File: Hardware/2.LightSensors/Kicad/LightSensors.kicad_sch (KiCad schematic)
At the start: 20 parts, among them J1 Conn_01x10_Pin, U1 AS7331, U2 OPT3004

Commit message: update footprints
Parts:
- H1, H2, H3, H4: footprint MountingHole:MountingHole_3.2mm_M3_ISO7380 -> MountingHole:MountingHole_3.2mm_M3
- J1: footprint Connector_JST:JST_PH_S10B-PH-K_1x10_P2.00mm_Horizontal -> Connector_JST:JST_PH_B10B-PH-SM4-TB_1x10-1MP_P2.00mm_Vertical
- R3, R6: footprint Capacitor_SMD:C_0402_1005Metric -> Resistor_SMD:R_0402_1005Metric
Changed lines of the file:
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@@
-    )
-  )
-  (symbol (lib_id "Mechanical:MountingHole") (at 64.77 193.04 0) (unit 1)
-    (in_bom yes) (on_board yes) (dnp no) (fields_autoplaced)
-    (property "Reference" "H2" (at 67.31 191.77 0)
-      (effects (font (size 1.27 1.27)) (justify left))
-    )
-    (property "Value" "MountingHole" (at 67.31 194.31 0)
-      (effects (font (size 1.27 1.27)) (justify left) hide)
-    )
-    (property "Footprint" "MountingHole:MountingHole_3.2mm_M3_ISO7380" (at 64.77 193.04 0)
-      (effects (font (size 1.27 1.27)) hide)
-    )
-    (property "Datasheet" "~" (at 64.77 193.04 0)
-      (effects (font (size 1.27 1.27)) hide)
-    )
-    (instances
-      (project "LightSensors"
-        (path "/23129930-610b-43a1-9ece-3793e6901ef4"
-          (reference "H2") (unit 1)
-        )
-      )
     )
   )
@@
     )
   )
-  (symbol (lib_id "Mechanical:MountingHole") (at 73.66 193.04 0) (unit 1)
-    (in_bom yes) (on_board yes) (dnp no) (fields_autoplaced)
-    (property "Reference" "H4" (at 76.2 191.77 0)
-      (effects (font (size 1.27 1.27)) (justify left))
-    )
-    (property "Value" "MountingHole" (at 76.2 194.31 0)
-      (effects (font (size 1.27 1.27)) (justify left) hide)
-    )
-    (property "Footprint" "MountingHole:MountingHole_3.2mm_M3_ISO7380" (at 73.66 193.04 0)
-      (effects (font (size 1.27 1.27)) hide)
-    )
-    (property "Datasheet" "~" (at 73.66 193.04 0)
-      (effects (font (size 1.27 1.27)) hide)
-    )
-    (instances
-      (project "LightSensors"
-        (path "/23129930-610b-43a1-9ece-3793e6901ef4"
-          (reference "H4") (unit 1)
-        )
-      )
-    )
-  )
   (symbol (lib_id "Device:C") (at 213.36 55.88 0) (unit 1)
     (in_bom yes) (on_board yes) (dnp no) (fields_autoplaced)
@@
         (path "/e35789fa-b5f2-47cd-8637-9150d2b422dd"
           (reference "C1") (unit 1)
+        )
+      )
+    )
+  )
+  (symbol (lib_id "Mechanical:MountingHole") (at 83.82 184.15 0) (unit 1)
+    (in_bom yes) (on_board yes) (dnp no) (fields_autoplaced)
+    (property "Reference" "H3" (at 86.36 182.88 0)
+      (effects (font (size 1.27 1.27)) (justify left))
+    )
+    (property "Value" "MountingHole" (at 86.36 185.42 0)
+      (effects (font (size 1.27 1.27)) (justify left))
+    )
+    (property "Footprint" "MountingHole:MountingHole_3.2mm_M3" (at 83.82 184.15 0)
+      (effects (font (size 1.27 1.27)) hide)
+    )
+    (property "Datasheet" "~" (at 83.82 184.15 0)
+      (effects (font (size 1.27 1.27)) hide)
+    )
+    (instances
+      (project "LightSensors"
+        (path "/23129930-610b-43a1-9ece-3793e6901ef4"
+          (reference "H3") (unit 1)
         )
       )
@@
     )
   )
+  (symbol (lib_id "Mechanical:MountingHole") (at 83.82 190.5 0) (unit 1)
+    (in_bom yes) (on_board yes) (dnp no) (fields_autoplaced)
+    (property "Reference" "H4" (at 86.36 189.23 0)
+      (effects (font (size 1.27 1.27)) (justify left))
+    )
+    (property "Value" "MountingHole" (at 86.36 191.77 0)
+      (effects (font (size 1.27 1.27)) (justify left))
+    )
+    (property "Footprint" "MountingHole:MountingHole_3.2mm_M3" (at 83.82 190.5 0)
+      (effects (font (size 1.27 1.27)) hide)
+    )
+    (property "Datasheet" "~" (at 83.82 190.5 0)
+      (effects (font (size 1.27 1.27)) hide)
+    )
+    (instances
+      (project "LightSensors"
+        (path "/23129930-610b-43a1-9ece-3793e6901ef4"
+          (reference "H4") (unit 1)
+        )
+      )
+    )
+  )
   (symbol (lib_id "power:+3.3V") (at 220.98 48.26 0) (unit 1)
     (in_bom yes) (on_board yes) (dnp no) (fields_autoplaced)
@@
     )
   )
-  (symbol (lib_id "Mechanical:MountingHole") (at 73.66 185.42 0) (unit 1)
-    (in_bom yes) (on_board yes) (dnp no) (fields_autoplaced)
-    (property "Reference" "H3" (at 76.2 184.15 0)
-      (effects (font (size 1.27 1.27)) (justify left))
-    )
-    (property "Value" "MountingHole" (at 76.2 186.69 0)
-      (effects (font (size 1.27 1.27)) (justify left) hide)
-    )
-    (property "Footprint" "MountingHole:MountingHole_3.2mm_M3_ISO7380" (at 73.66 185.42 0)
-      (effects (font (size 1.27 1.27)) hide)
-    )
-    (property "Datasheet" "~" (at 73.66 185.42 0)
-      (effects (font (size 1.27 1.27)) hide)
-    )
-    (instances
-      (project "LightSensors"
-        (path "/23129930-610b-43a1-9ece-3793e6901ef4"
-          (reference "H3") (unit 1)
-        )
-      )
-    )
-  )
   (symbol (lib_id "power:+3.3VA") (at 83.82 31.75 0) (unit 1)
     (in_bom yes) (on_board yes) (dnp no) (fields_autoplaced)
@@
       (effects (font (size 1.27 1.27)) (justify left))
     )
-    (property "Footprint" "Capacitor_SMD:C_0402_1005Metric" (at 254.762 44.45 90)
+    (property "Footprint" "Resistor_SMD:R_0402_1005Metric" (at 254.762 44.45 90)
       (effects (font (size 1.27 1.27)) hide)
     )
@@
     )
   )
+  (symbol (lib_id "Mechanical:MountingHole") (at 64.77 184.15 0) (unit 1)
+    (in_bom yes) (on_board yes) (dnp no) (fields_autoplaced)
+    (property "Reference" "H1" (at 67.31 182.88 0)
+      (effects (font (size 1.27 1.27)) (justify left))
+    )
+    (property "Value" "MountingHole" (at 67.31 185.42 0)
+      (effects (font (size 1.27 1.27)) (justify left))
+    )
+    (property "Footprint" "MountingHole:MountingHole_3.2mm_M3" (at 64.77 184.15 0)
+      (effects (font (size 1.27 1.27)) hide)
+    )
+    (property "Datasheet" "~" (at 64.77 184.15 0)
+      (effects (font (size 1.27 1.27)) hide)
+    )
+    (instances
+      (project "LightSensors"
+        (path "/23129930-610b-43a1-9ece-3793e6901ef4"
+          (reference "H1") (unit 1)
+        )
+      )
+    )
+  )
   (symbol (lib_id "power:+3.3VA") (at 95.25 31.75 0) (unit 1)
     (in_bom yes) (on_board yes) (dnp no) (fields_autoplaced)
@@
       (effects (font (size 1.27 1.27)) (justify left))
     )
-    (property "Footprint" "Capacitor_SMD:C_0402_1005Metric" (at 123.952 54.61 90)
+    (property "Footprint" "Resistor_SMD:R_0402_1005Metric" (at 123.952 54.61 90)
       (effects (font (size 1.27 1.27)) hide)
     )
@@
     )
   )
-  (symbol (lib_id "Mechanical:MountingHole") (at 64.77 185.42 0) (unit 1)
-    (in_bom yes) (on_board yes) (dnp no) (fields_autoplaced)
-    (property "Reference" "H1" (at 67.31 184.15 0)
-      (effects (font (size 1.27 1.27)) (justify left))
-    )
-    (property "Value" "MountingHole" (at 67.31 186.69 0)
-      (effects (font (size 1.27 1.27)) (justify left) hide)
-    )
-    (property "Footprint" "MountingHole:MountingHole_3.2mm_M3_ISO7380" (at 64.77 185.42 0)
-      (effects (font (size 1.27 1.27)) hide)
-    )
-    (property "Datasheet" "~" (at 64.77 185.42 0)
-      (effects (font (size 1.27 1.27)) hide)
-    )
-    (instances
-      (project "LightSensors"
-        (path "/23129930-610b-43a1-9ece-3793e6901ef4"
-          (reference "H1") (unit 1)
-        )
-      )
-    )
-  )
   (symbol (lib_id "Device:R") (at 170.18 71.12 270) (unit 1)
     (in_bom yes) (on_board yes) (dnp no)
@@
       (effects (font (size 1.27 1.27)) hide)
     )
-    (property "Footprint" "Connector_JST:JST_PH_S10B-PH-K_1x10_P2.00mm_Horizontal" (at 25.4 52.07 0)
+    (property "Footprint" "Connector_JST:JST_PH_B10B-PH-SM4-TB_1x10-1MP_P2.00mm_Vertical" (at 25.4 52.07 0)
       (effects (font (size 1.27 1.27)) hide)
     )
@@
         )
       )
+    )
+  )
+  (symbol (lib_id "Mechanical:MountingHole") (at 64.77 190.5 0) (unit 1)
+    (in_bom yes) (on_board yes) (dnp no) (fields_autoplaced)
+    (property "Reference" "H2" (at 67.31 189.23 0)
+      (effects (font (size 1.27 1.27)) (justify left))
+    )
+    (property "Value" "MountingHole" (at 67.31 191.77 0)
+      (effects (font (size 1.27 1.27)) (justify left))
+    )
+    (property "Footprint" "MountingHole:MountingHole_3.2mm_M3" (at 64.77 190.5 0)
+      (effects (font (size 1.27 1.27)) hide)
+    )
+    (property "Datasheet" "~" (at 64.77 190.5 0)
+      (effects (font (size 1.27 1.27)) hide)
+    )
+    (instances
+      (project "LightSensors"
+        (path "/23129930-610b-43a1-9ece-3793e6901ef4"
+          (reference "H2") (unit 1)
+        )
+      )

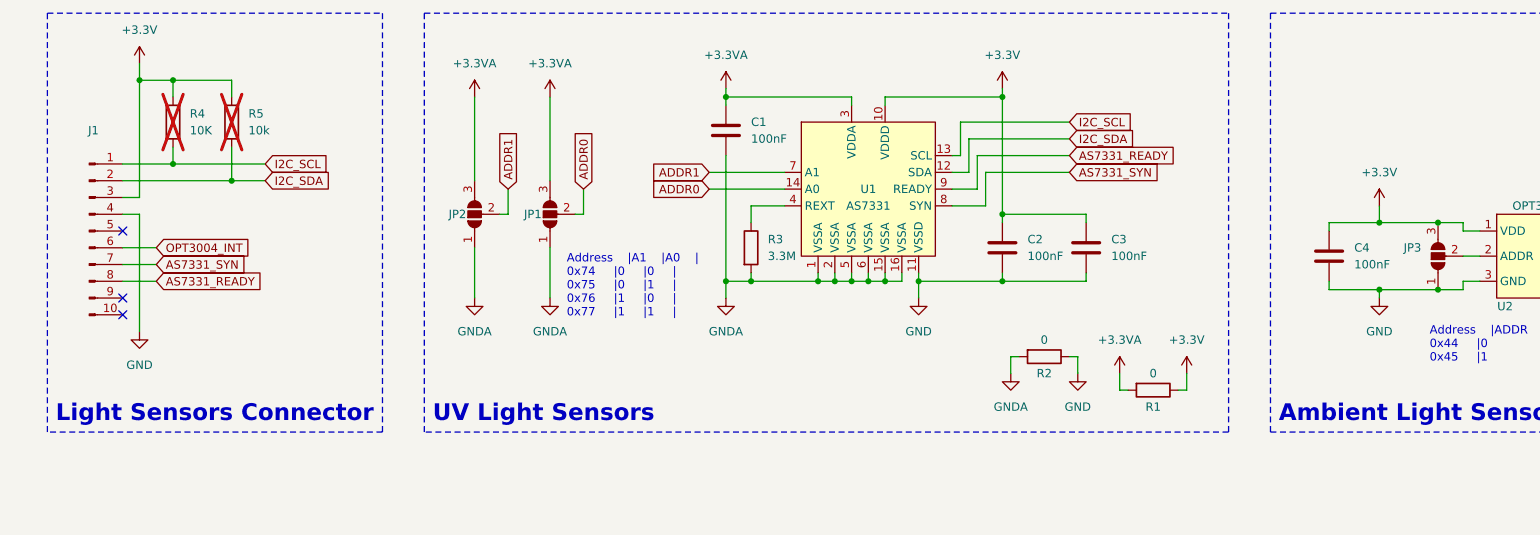
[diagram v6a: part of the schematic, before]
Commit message: Update pcb due to connector pinout fix
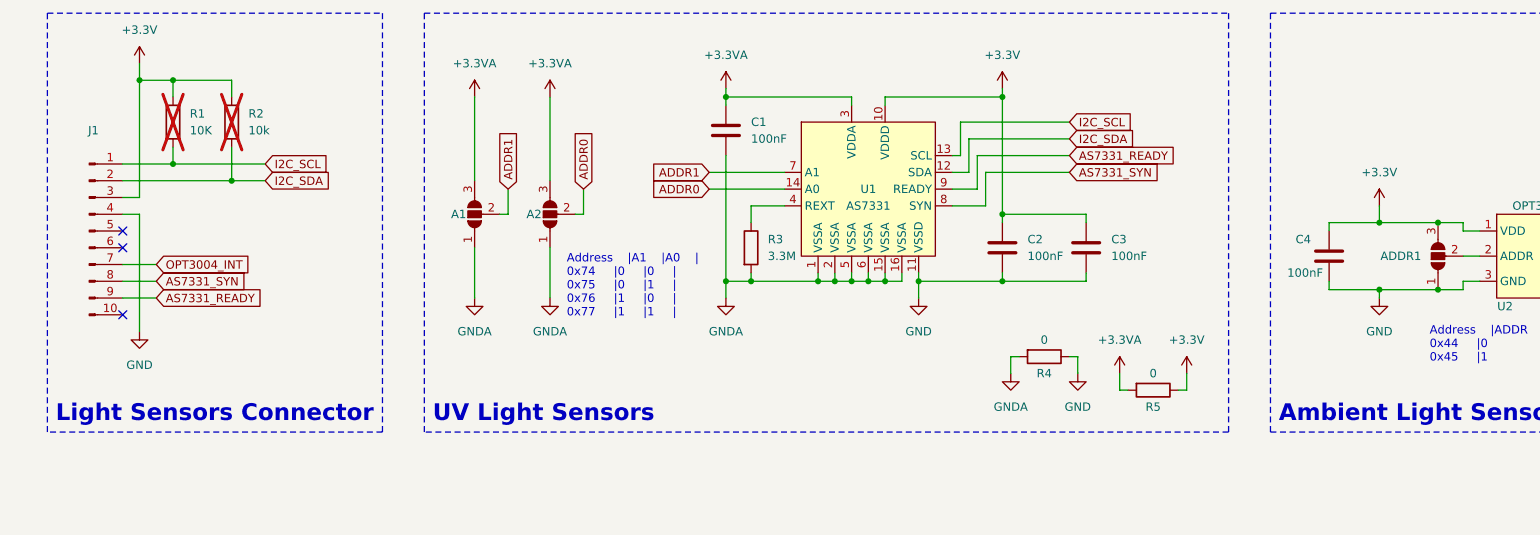
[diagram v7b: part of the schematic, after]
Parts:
- renumbered JP2 to A1, JP1 to A2, JP3 to ADDR1, R4 to R1, R5 to R2, R2 to R4, R1 to R5
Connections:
- net AS7331_READY: now also J1.9 (Pin_9); no longer J1.8 (Pin_8)
- net AS7331_SYN: now also J1.8 (Pin_8); no longer J1.7 (Pin_7)
- net OPT3004_INT: now also J1.7 (Pin_7); no longer J1.6 (Pin_6)

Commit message: Change footprints for resistors, capasitors and change mounting holes to M2
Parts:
- C1, C2, C3, C4: footprint Capacitor_SMD:C_0402_1005Metric -> Capacitor_SMD:C_0603_1608Metric
- H1, H2, H3, H4: footprint MountingHole:MountingHole_3.2mm_M3 -> MountingHole:MountingHole_2.2mm_M2
- R1, R2, R3: footprint Resistor_SMD:R_0402_1005Metric -> Resistor_SMD:R_0603_1608Metric
- R6: footprint Resistor_SMD:R_0402_1005Metric -> Capacitor_SMD:C_0603_1608Metric
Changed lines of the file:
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@@
       (effects (font (size 1.27 1.27)) (justify left))
     )
-    (property "Footprint" "Capacitor_SMD:C_0402_1005Metric" (at 214.3252 59.69 0)
+    (property "Footprint" "Capacitor_SMD:C_0603_1608Metric" (at 214.3252 59.69 0)
       (effects (font (size 1.27 1.27)) hide)
     )
@@
       (effects (font (size 1.27 1.27)) (justify left))
     )
-    (property "Footprint" "MountingHole:MountingHole_3.2mm_M3" (at 83.82 184.15 0)
+    (property "Footprint" "MountingHole:MountingHole_2.2mm_M2" (at 83.82 184.15 0)
       (effects (font (size 1.27 1.27)) hide)
     )
@@
       (effects (font (size 1.27 1.27)) (justify left))
     )
-    (property "Footprint" "Capacitor_SMD:C_0402_1005Metric" (at 177.4952 58.42 0)
+    (property "Footprint" "Capacitor_SMD:C_0603_1608Metric" (at 177.4952 58.42 0)
       (effects (font (size 1.27 1.27)) hide)
     )
@@
       (effects (font (size 1.27 1.27)) (justify left))
     )
-    (property "Footprint" "MountingHole:MountingHole_3.2mm_M3" (at 83.82 190.5 0)
+    (property "Footprint" "MountingHole:MountingHole_2.2mm_M2" (at 83.82 190.5 0)
       (effects (font (size 1.27 1.27)) hide)
     )
@@
       (effects (font (size 1.27 1.27)) (justify left))
     )
-    (property "Footprint" "Capacitor_SMD:C_0402_1005Metric" (at 164.7952 58.42 0)
+    (property "Footprint" "Capacitor_SMD:C_0603_1608Metric" (at 164.7952 58.42 0)
       (effects (font (size 1.27 1.27)) hide)
     )
@@
       (effects (font (size 1.27 1.27)) (justify left))
     )
-    (property "Footprint" "Resistor_SMD:R_0402_1005Metric" (at 45.212 35.56 90)
+    (property "Footprint" "Resistor_SMD:R_0603_1608Metric" (at 45.212 35.56 90)
       (effects (font (size 1.27 1.27)) hide)
     )
@@
       (effects (font (size 1.27 1.27)) (justify left))
     )
-    (property "Footprint" "Resistor_SMD:R_0402_1005Metric" (at 36.322 35.56 90)
+    (property "Footprint" "Resistor_SMD:R_0603_1608Metric" (at 36.322 35.56 90)
       (effects (font (size 1.27 1.27)) hide)
     )
@@
       (effects (font (size 1.27 1.27)) (justify left))
     )
-    (property "Footprint" "Resistor_SMD:R_0402_1005Metric" (at 254.762 44.45 90)
+    (property "Footprint" "Capacitor_SMD:C_0603_1608Metric" (at 254.762 44.45 90)
       (effects (font (size 1.27 1.27)) hide)
     )
@@
       (effects (font (size 1.27 1.27)) (justify left))
     )
-    (property "Footprint" "MountingHole:MountingHole_3.2mm_M3" (at 64.77 184.15 0)
+    (property "Footprint" "MountingHole:MountingHole_2.2mm_M2" (at 64.77 184.15 0)
       (effects (font (size 1.27 1.27)) hide)
     )
@@
       (effects (font (size 1.27 1.27)) (justify left))
     )
-    (property "Footprint" "Capacitor_SMD:C_0402_1005Metric" (at 122.8852 40.64 0)
+    (property "Footprint" "Capacitor_SMD:C_0603_1608Metric" (at 122.8852 40.64 0)
       (effects (font (size 1.27 1.27)) hide)
     )
@@
       (effects (font (size 1.27 1.27)) (justify left))
     )
-    (property "Footprint" "Resistor_SMD:R_0402_1005Metric" (at 123.952 54.61 90)
+    (property "Footprint" "Resistor_SMD:R_0603_1608Metric" (at 123.952 54.61 90)
       (effects (font (size 1.27 1.27)) hide)
     )
@@
       (effects (font (size 1.27 1.27)) (justify left))
     )
-    (property "Footprint" "MountingHole:MountingHole_3.2mm_M3" (at 64.77 190.5 0)
-      (effects (font (size 1.27 1.27)) hide)
-    )
+    (property "Footprint" "MountingHole:MountingHole_2.2mm_M2" (at 64.77 190.5 0)
+      (effects (font (size 1.27 1.27)) hide)
+    )
